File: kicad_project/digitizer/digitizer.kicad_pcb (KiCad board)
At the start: 2 copper layers, 96 x 74 mm, 63 parts, among them IC201 MAX3059ASA+T UPSTREAM, IC202 MAX6035AAUR50+T, IC203 MAX3059ASA+T DOWNSTREAM, IC204 MAX6043BAUT33+T, IC301 ADS1234IPWR, J201 DT15-4P (UPSTREAM), J202 DT06-4S (DOWNSTREAM), J301 Load Cell 1, J302 Load Cell 2, J303 Load Cell 3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

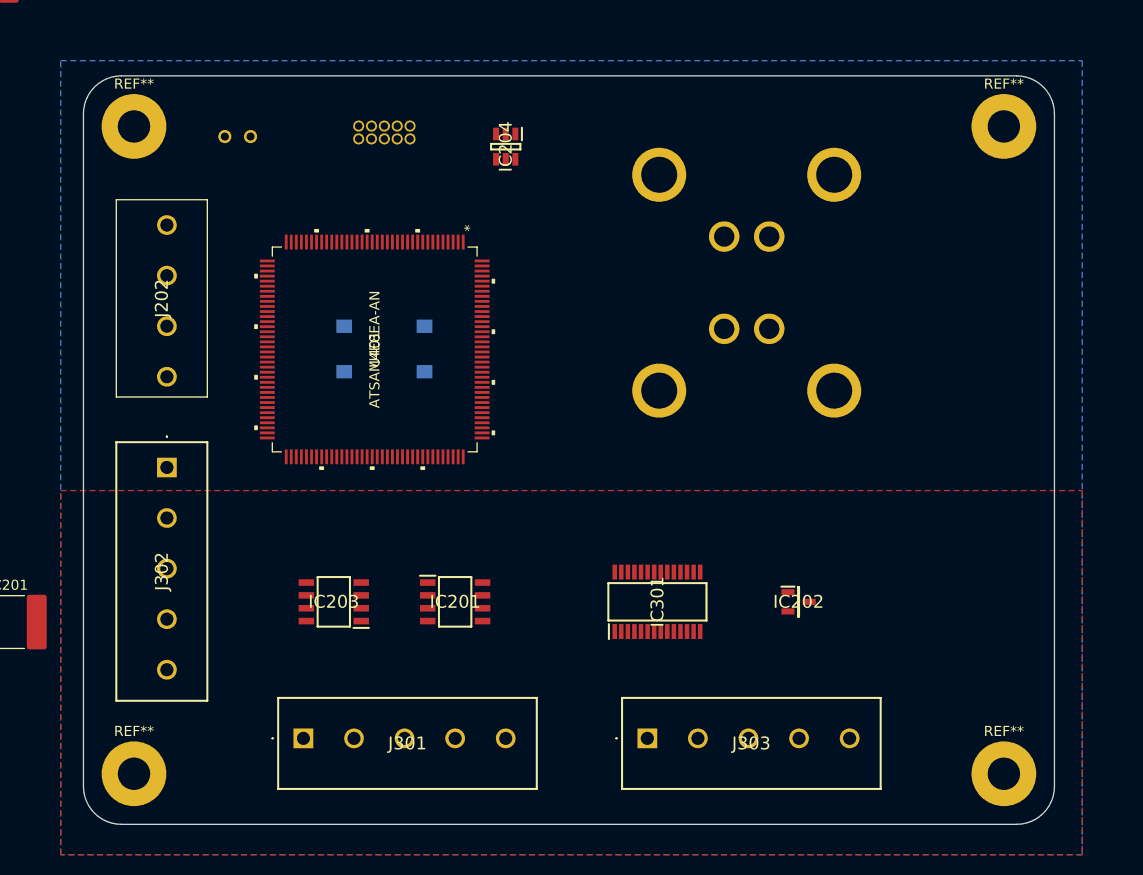
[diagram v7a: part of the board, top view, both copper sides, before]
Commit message: added 12V_CLEAN label to schematic; added planes for 12V_CLEAN and 3V3_CLEAN to layout
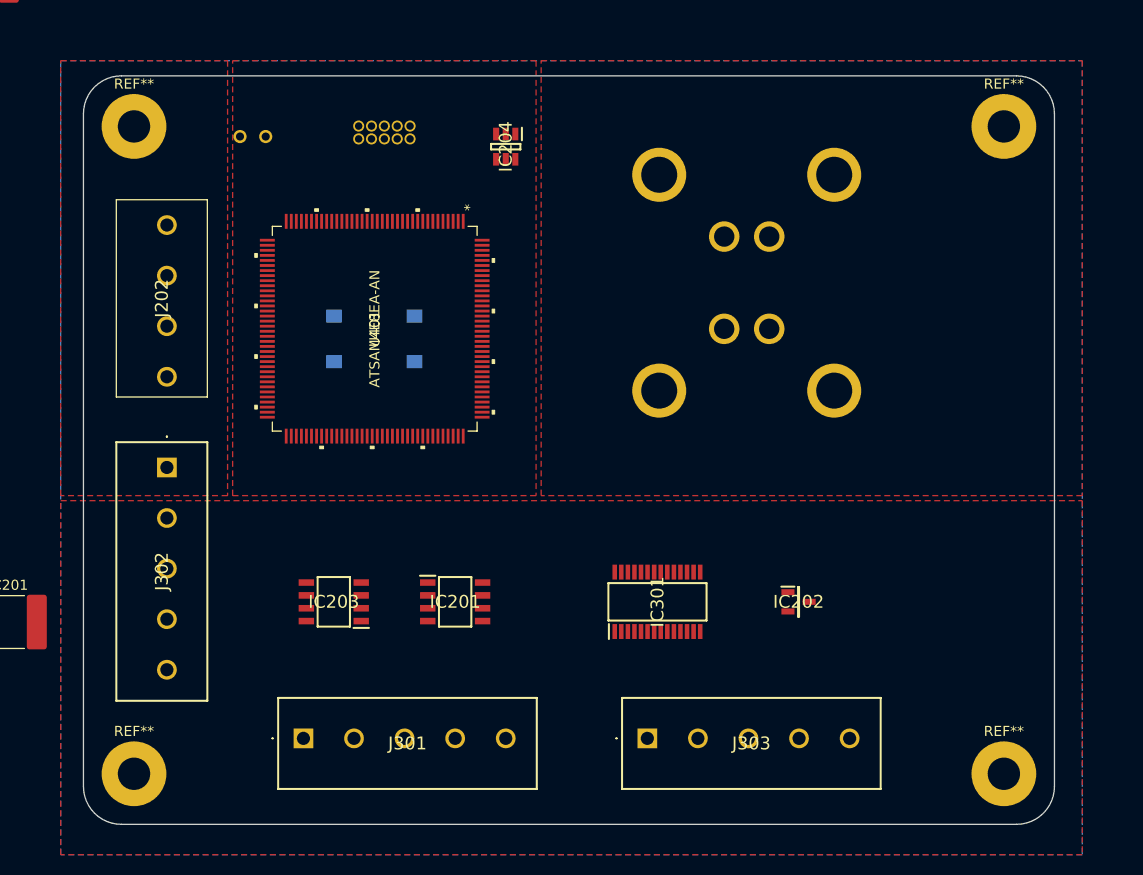
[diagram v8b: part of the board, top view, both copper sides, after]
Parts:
- moved U401 2.05 mm to (103.0, 74.0)
- moved LED201 1.50 mm to (91.0, 55.0)
- moved S401 1.41 mm to (103.0, 75.0)
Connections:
- net Net-(C201-Pad1) renamed 12V_CLEAN
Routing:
- added copper zone on F.Cu, net 12V_CLEAN
- added copper zone on F.Cu, net 3V3_CLEAN
